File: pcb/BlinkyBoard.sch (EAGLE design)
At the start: 24 parts, among them Q1 16 MHz

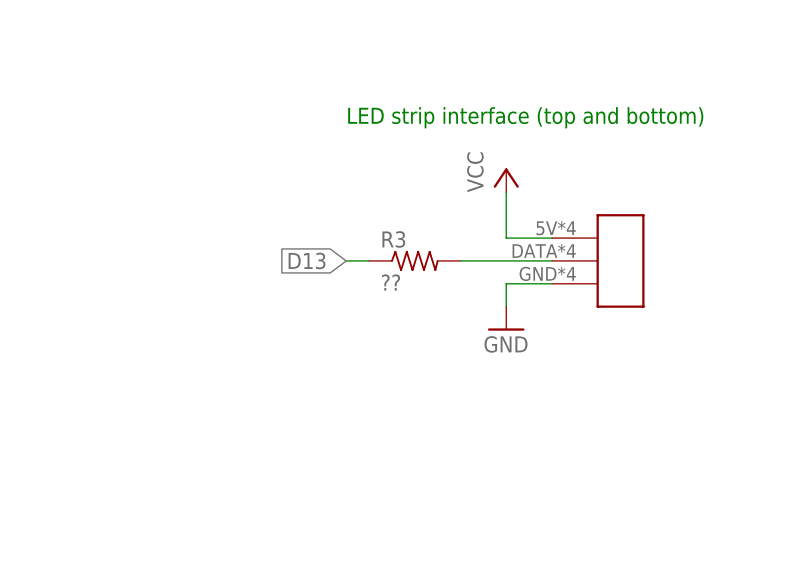
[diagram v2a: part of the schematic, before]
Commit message: Fix output resistor value
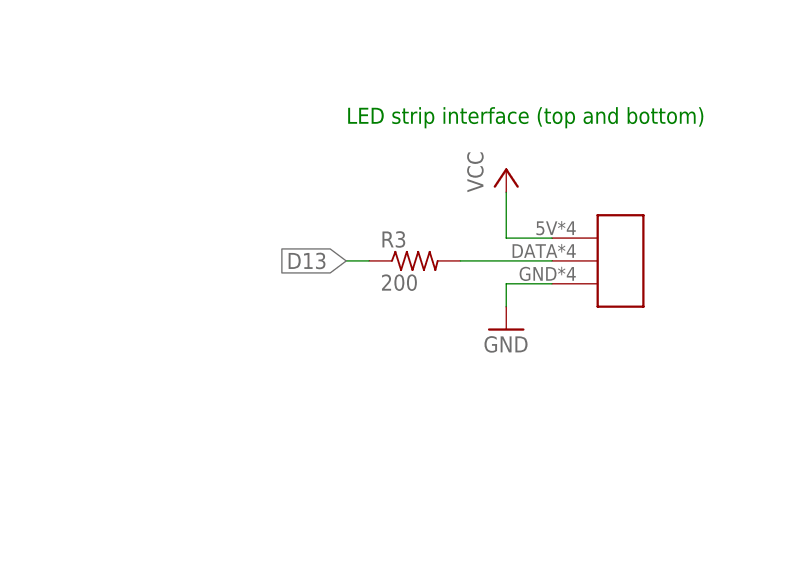
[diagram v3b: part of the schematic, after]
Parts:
- R3: value ?? -> 200
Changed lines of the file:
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@@
 <?xml version="1.0" encoding="utf-8"?>
 <!DOCTYPE eagle SYSTEM "eagle.dtd">
-<eagle version="7.2.0">
+<eagle version="7.5.0">
 <drawing>
 <settings>
@@
 <part name="GND9" library="supply1" deviceset="GND" device=""/>
 <part name="U$9" library="blinkiverse" deviceset="WS2812B_CONNECTOR" device=""/>
-<part name="R3" library="blinkiverse" deviceset="R_US" device="" value="??"/>
+<part name="R3" library="blinkiverse" deviceset="R_US" device="" value="200"/>
 <part name="U$7" library="blinkinlabs" deviceset="BUTTON_MOMENTARY" device=""/>
 </parts>

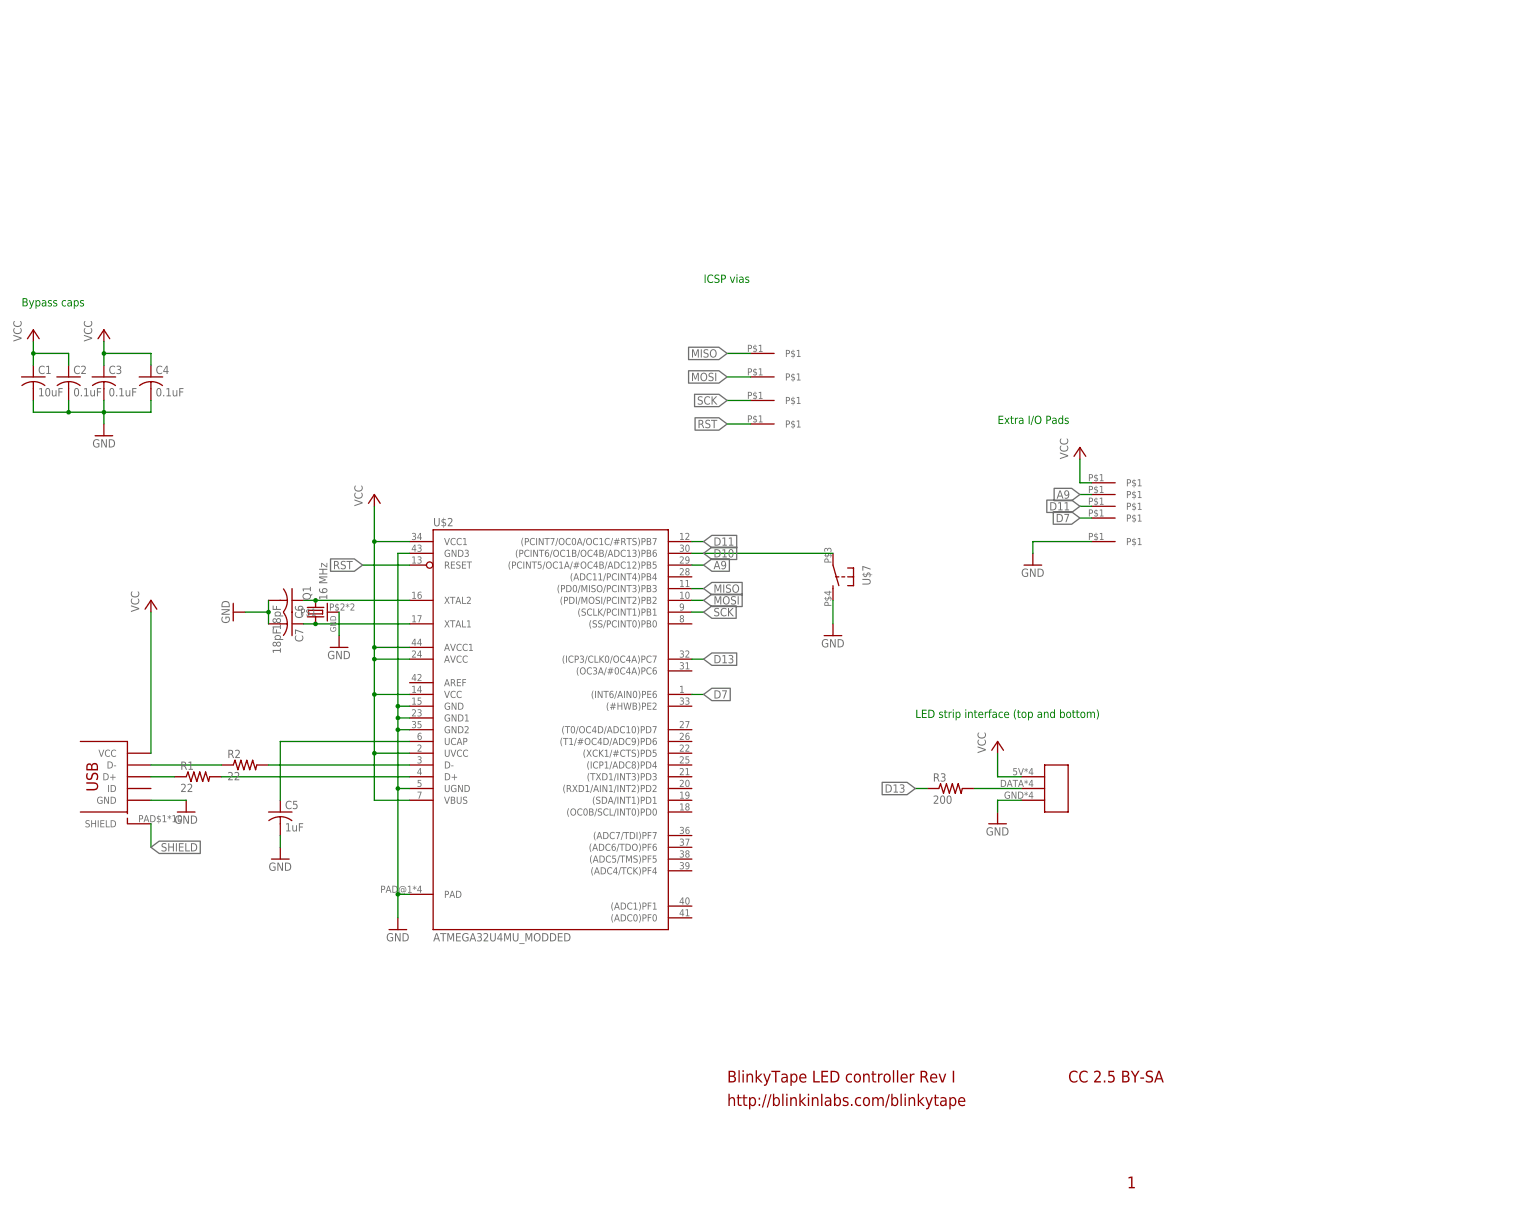
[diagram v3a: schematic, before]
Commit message: Add ESD components, needs routing
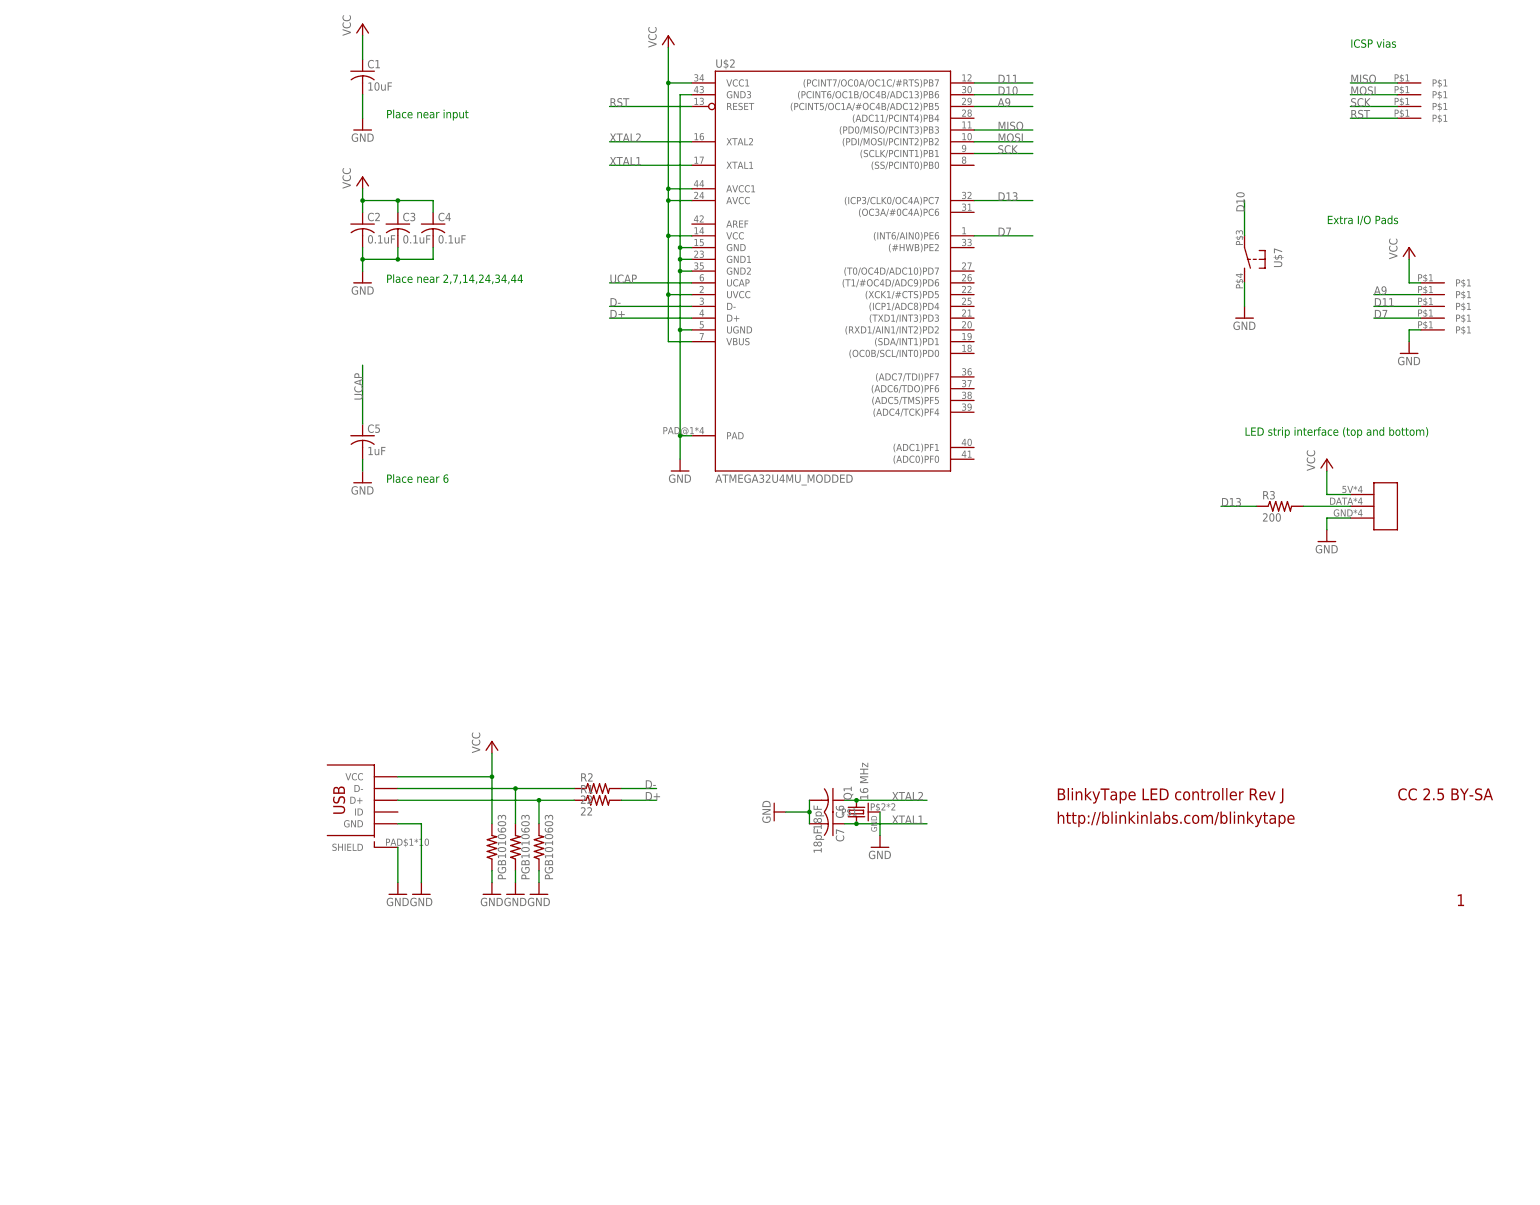
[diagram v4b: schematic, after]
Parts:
- added Z1, Z2, Z3: PGB1010603, PaxInstrument-T400:SPARKFUN-RESISTORS_RESISTOR0603-RES
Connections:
- net N$2 renamed UCAP
- net N$8 renamed XTAL2
- net N$9 renamed XTAL1
- removed net SHIELD: U$4.SHIELD
- net D+_IN: now also Z1.2
- net D-_IN: now also Z2.2
- net GND: now also U$4.SHIELD, Z1.1, Z2.1, Z3.1
- net VCC: now also Z3.2
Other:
- note added: "BlinkyTape LED controller Rev J"
- note added: "Place near 2,7,14,24,34,44"
- note added: "Place near 6"
- note added: "Place near input"
- note removed: "BlinkyTape LED controller Rev I"
- note removed: "Bypass caps"
- moved on the sheet: C1, C2, C3, C4, C5, C6, C7, Q1, R1, R2, R3, U$2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

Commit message: Update schematic
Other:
- note added: "Atmega 32u4"
- note added: "BlinkyTape Controller"
- note added: "Copyright 2013-2016 Blinkinlabs, LLC"
- note added: "Extra I/O"
- note added: "LED control over serial, ATMEGA programming using Caterina bootloader"
- note added: "LED strip connector"
- note added: "Main microcontroller"
- note added: "Pushbutton switch"
- note added: "Revision Notes/Changelog Revision I: -Add ESD protection diodes -Switch to slightly smaller process (.2 via, 7mil spacing) TODO: -Find smaller ESD component, finish routing"
- note added: "This documentation describes Open Hardware and is licensed under the CERN OHL v. 1.2. You may redistribute and modify this documentation under the terms of the CERN OHL v.1.2. (http://ohwr.org/cernohl). This documentation is distributed WITHOUT ANY EXPRESS OR IMPLIED WARRANTY, INCLUDING OF MERCHANTABILITY, SATISFACTORY QUALITY AND FITNESS FOR A PARTICULAR PURPOSE. Please see the CERN OHL v.1.2 fo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"
- note added: "USB port"
- note removed: "1"
- note removed: "BlinkyTape LED controller Rev J"
- note removed: "CC 2.5 BY-SA"
- note removed: "Extra I/O Pads"
- note removed: "LED strip interface (top and bottom)"
- note removed: "http://blinkinlabs.com/blinkytape"
